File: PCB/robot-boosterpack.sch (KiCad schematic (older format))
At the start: 17 parts

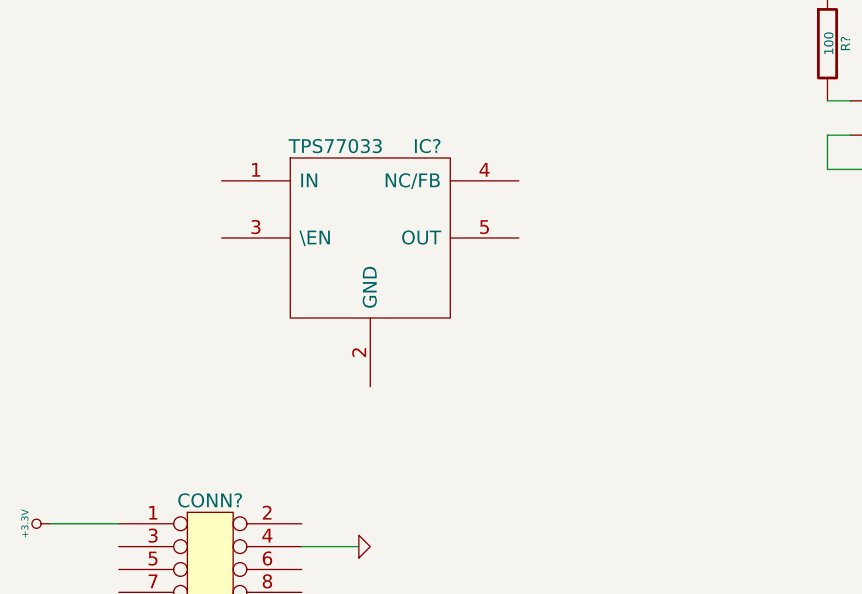
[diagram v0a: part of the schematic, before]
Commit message: created 3.3V regulator circuit
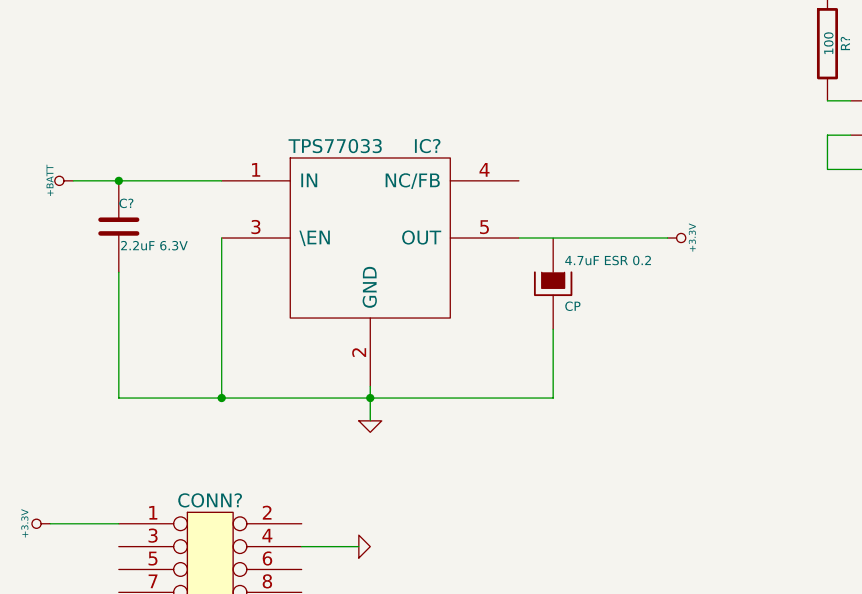
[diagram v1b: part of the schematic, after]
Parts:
- added 4.7uF: CP, symbol CP
- added C?: 2.2uF 6.3V, ~, symbol C
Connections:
- wire segments 43 -> 50
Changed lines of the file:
@@
 	1    0    0    -1
 $EndComp
+$Comp
+L C C?
+U 1 1 53A8AF20
+P 3600 1850
+F 0 "C?" H 3600 1950 40  0000 L CNN
+F 1 "2.2uF 6.3V" H 3606 1765 40  0000 L CNN
+F 2 "~" H 3638 1700 30  0000 C CNN
+F 3 "~" H 3600 1850 60  0000 C CNN
+	1    3600 1850
+	1    0    0    -1
+$EndComp
+Wire Wire Line
+	3400 1650 4050 1650
+Connection ~ 3600 1650
+Wire Wire Line
+	4700 2550 4700 2700
+Wire Wire Line
+	3600 2600 5500 2600
+Wire Wire Line
+	3600 2600 3600 2050
+Wire Wire Line
+	4050 1900 4050 2600
+Connection ~ 4050 2600
+$Comp
+L GND #PWR?
+U 1 1 53A8B23A
+P 4700 2700
+F 0 "#PWR?" H 4700 2700 30  0001 C CNN
+F 1 "GND" H 4700 2630 30  0001 C CNN
+F 2 "" H 4700 2700 60  0000 C CNN
+F 3 "" H 4700 2700 60  0000 C CNN
+	1    4700 2700
+	1    0    0    -1
+$EndComp
+Connection ~ 4700 2600
+Wire Wire Line
+	5350 1900 6000 1900
+$Comp
+L CP 4.7uF
+U 1 1 53A8B338
+P 5500 2100
+F 0 "4.7uF ESR 0.2" H 5550 2200 40  0000 L CNN
+F 1 "CP" H 5550 2000 40  0000 L CNN
+F 2 "" H 5600 1950 30  0000 C CNN
+F 3 "" H 5500 2100 300 0000 C CNN
+	1    5500 2100
+	1    0    0    -1
+$EndComp
+Wire Wire Line
+	5500 2600 5500 2300
+$Comp
+L +BATT #PWR?
+U 1 1 53A8B63C
+P 3400 1650
+F 0 "#PWR?" H 3400 1600 20  0001 C CNN
+F 1 "+BATT" H 3400 1750 30  0000 C CNN
+F 2 "" H 3400 1650 60  0000 C CNN
+F 3 "" H 3400 1650 60  0000 C CNN
+	1    3400 1650
+	0    -1   -1   0
+$EndComp
+$Comp
+L +3.3V #PWR?
+U 1 1 53A8B835
+P 6000 1900
+F 0 "#PWR?" H 6000 1860 30  0001 C CNN
+F 1 "+3.3V" H 6000 2010 30  0000 C CNN
+F 2 "" H 6000 1900 60  0000 C CNN
+F 3 "" H 6000 1900 60  0000 C CNN
+	1    6000 1900
+	0    1    1    0
+$EndComp
 $EndSCHEMATC

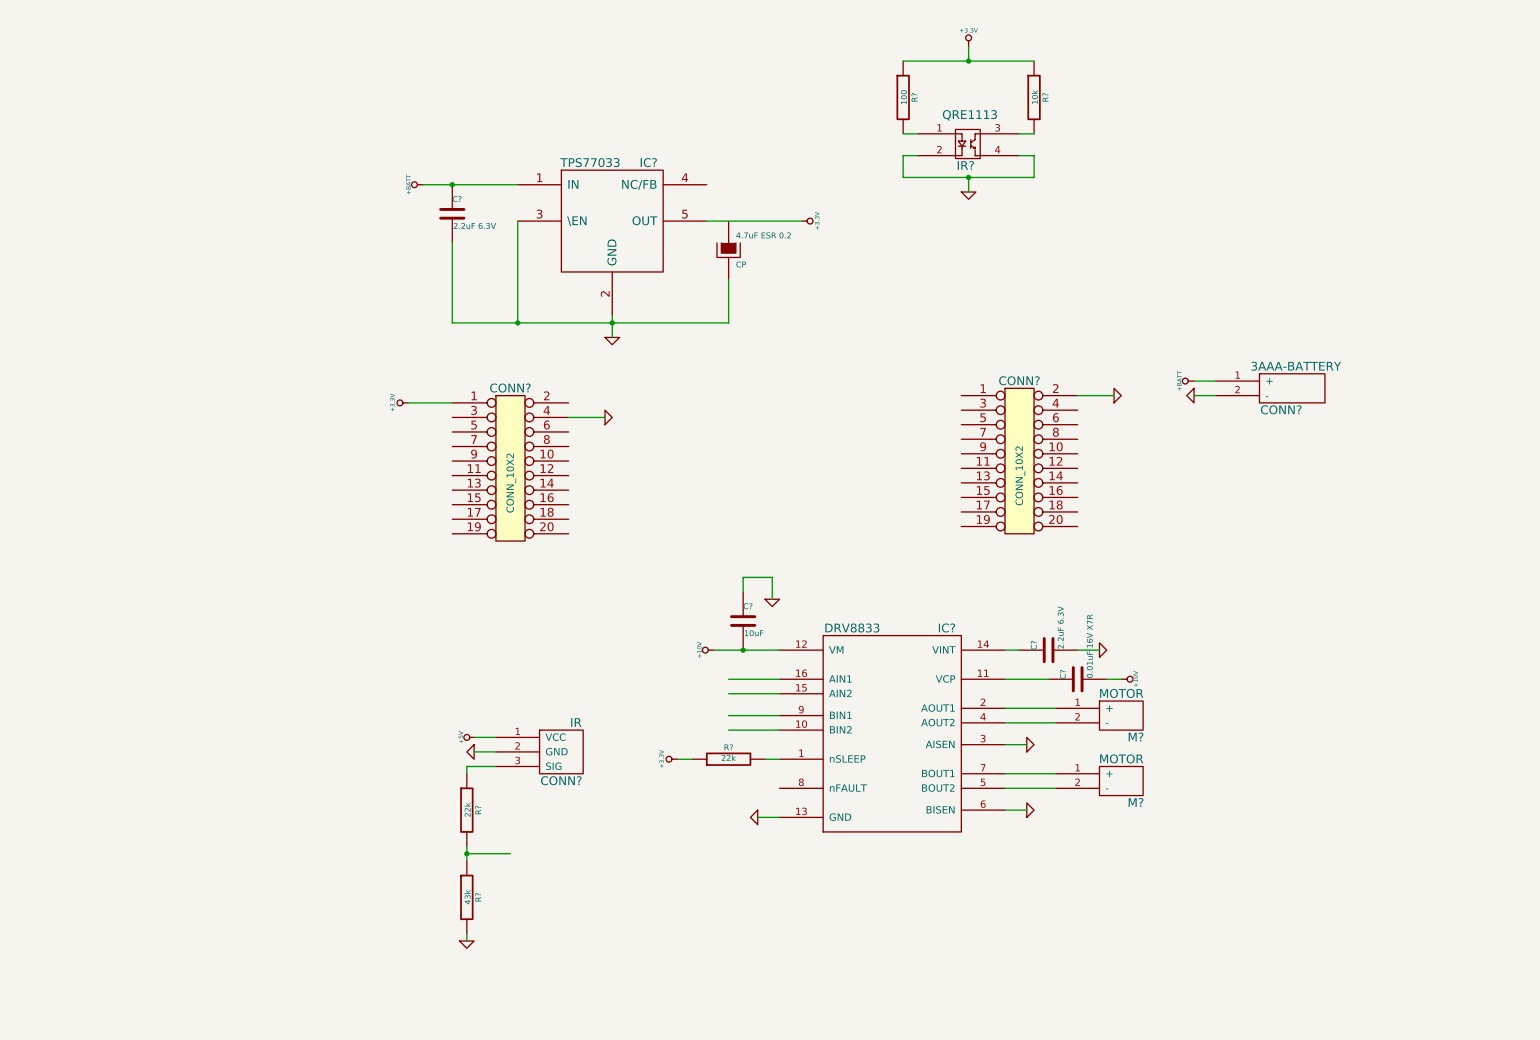
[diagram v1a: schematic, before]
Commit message: created 10V regulator schematic
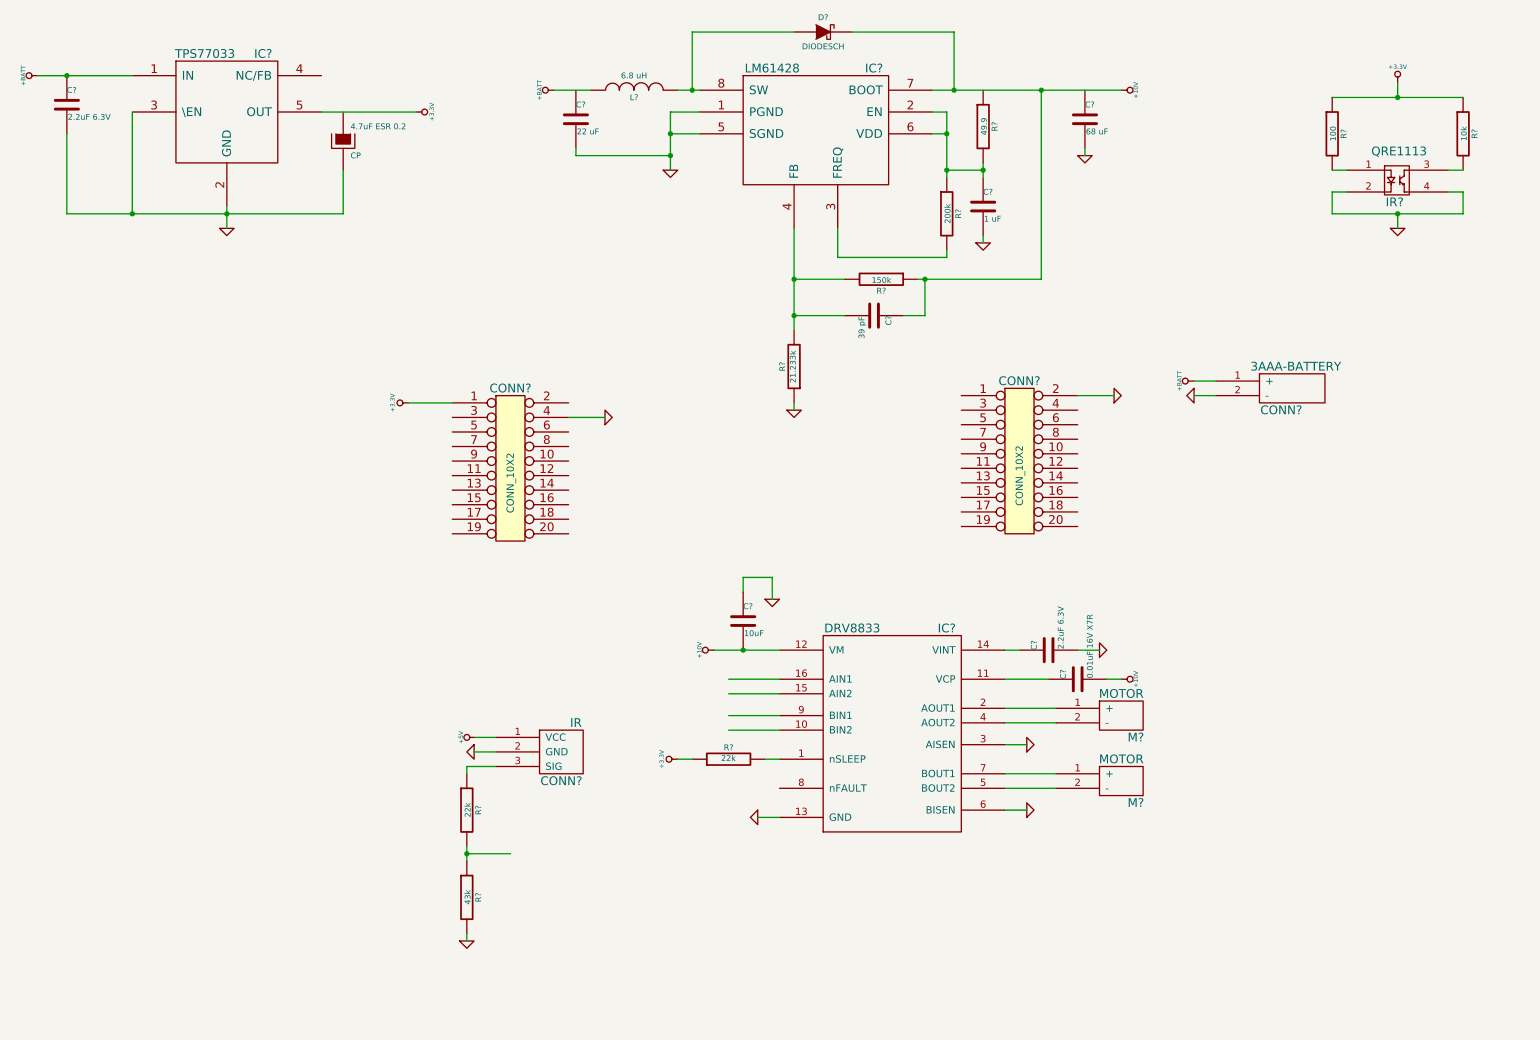
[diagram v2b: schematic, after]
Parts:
- added C?: 22 uF, ~, symbol C
- added C?: 1 uF, ~, symbol C
- added C?: 39 pF, ~, symbol C
- added C?: 68 uF, ~, symbol C
- added D?: DIODESCH, symbol DIODESCH
- added IC?: LM61428, symbol LM61428
- added L?: 6.8 uH, symbol INDUCTOR
- added R?: 49.9, ~, symbol R
- added R?: 200k, ~, symbol R
- added R?: 150k, ~, symbol R
- added R?: 21.233k, ~, symbol R
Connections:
- wire segments 50 -> 80
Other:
- moved on the sheet: 4.7uF ESR 0.2, C?, IC?, IR?, R?

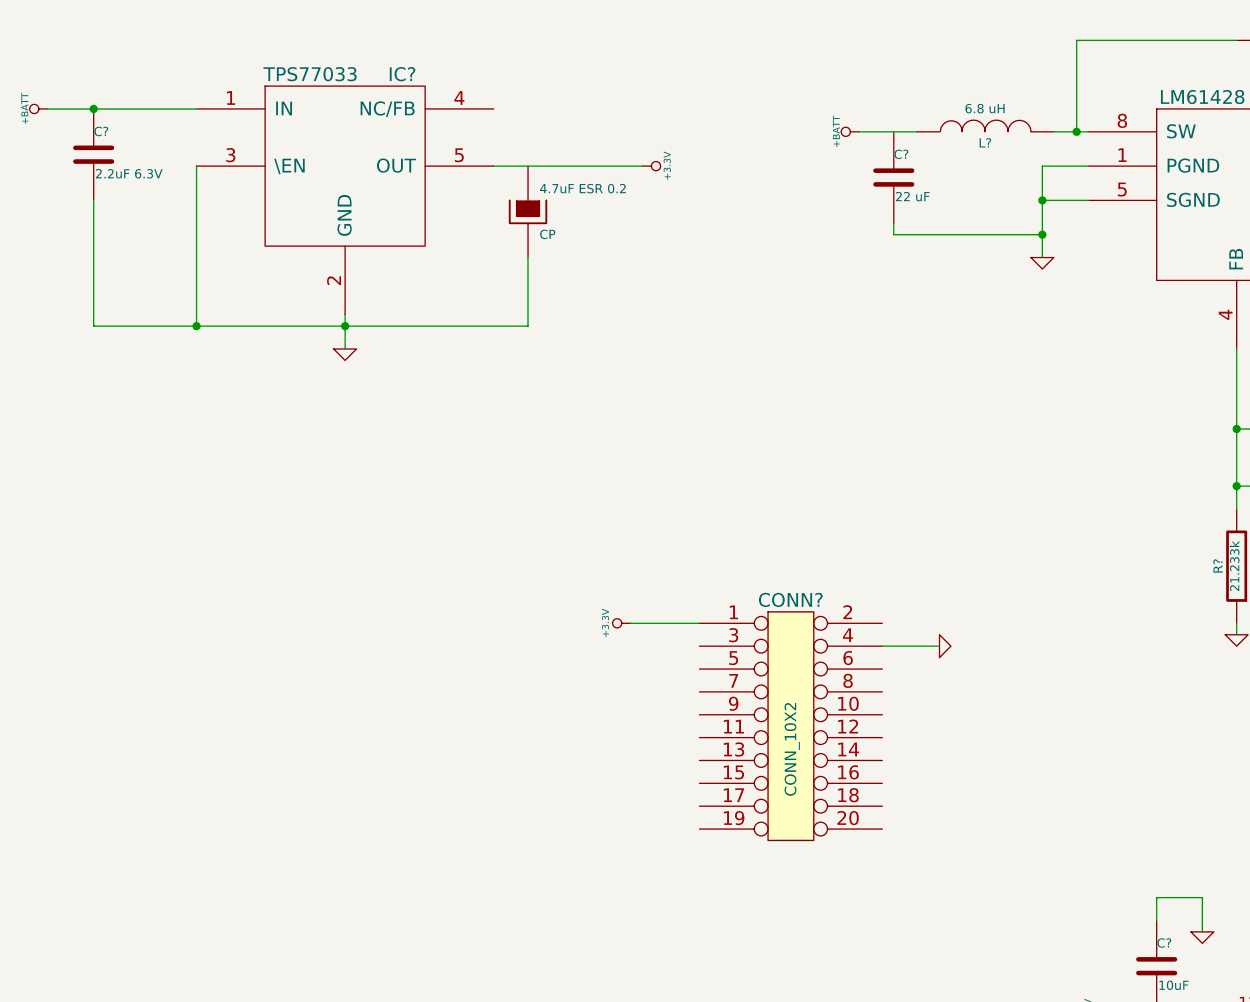
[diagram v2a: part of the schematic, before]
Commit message: added 5V regulator circuit
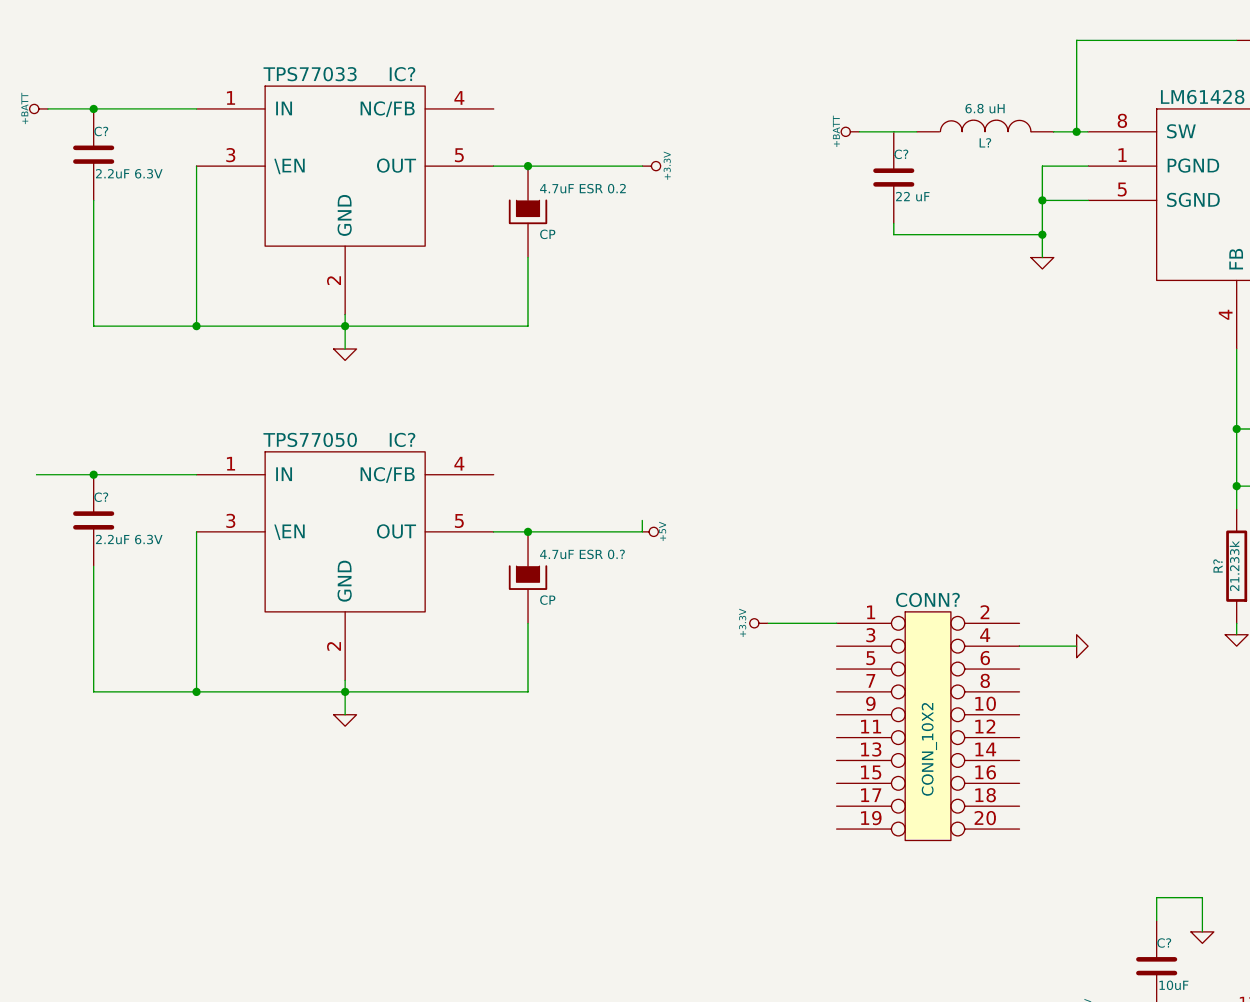
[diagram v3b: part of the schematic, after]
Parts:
- added 4.7uF~ESR~0.?: CP, symbol CP
- added C?: 2.2uF 6.3V, ~, symbol C
- added IC?: TPS77050, symbol TPS77050
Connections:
- wire segments 80 -> 88
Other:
- moved on the sheet: CONN?
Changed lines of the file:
@@
 L CONN_10X2 CONN?
 U 1 1 53A20530
-P 4000 3600
-F 0 "CONN?" H 4000 4150 60  0000 C CNN
-F 1 "CONN_10X2" V 4000 3500 50  0000 C CNN
-F 2 "" H 4000 3600 60  0000 C CNN
-F 3 "" H 4000 3600 60  0000 C CNN
-	1    4000 3600
+P 4600 3600
+F 0 "CONN?" H 4600 4150 60  0000 C CNN
+F 1 "CONN_10X2" V 4600 3500 50  0000 C CNN
+F 2 "" H 4600 3600 60  0000 C CNN
+F 3 "" H 4600 3600 60  0000 C CNN
+	1    4600 3600
 	1    0    0    -1
 $EndComp
@@
 L +3.3V #PWR?
 U 1 1 53A7389D
-P 3300 3150
-F 0 "#PWR?" H 3300 3110 30  0001 C CNN
-F 1 "+3.3V" H 3300 3260 30  0000 C CNN
-F 2 "" H 3300 3150 60  0000 C CNN
-F 3 "" H 3300 3150 60  0000 C CNN
-	1    3300 3150
+P 3900 3150
+F 0 "#PWR?" H 3900 3110 30  0001 C CNN
+F 1 "+3.3V" H 3900 3260 30  0000 C CNN
+F 2 "" H 3900 3150 60  0000 C CNN
+F 3 "" H 3900 3150 60  0000 C CNN
+	1    3900 3150
 	0    -1   -1   0
 $EndComp
@@
 L GND #PWR?
 U 1 1 53A738AC
-P 4650 3250
-F 0 "#PWR?" H 4650 3250 30  0001 C CNN
-F 1 "GND" H 4650 3180 30  0001 C CNN
-F 2 "" H 4650 3250 60  0000 C CNN
-F 3 "" H 4650 3250 60  0000 C CNN
-	1    4650 3250
+P 5250 3250
+F 0 "#PWR?" H 5250 3250 30  0001 C CNN
+F 1 "GND" H 5250 3180 30  0001 C CNN
+F 2 "" H 5250 3250 60  0000 C CNN
+F 3 "" H 5250 3250 60  0000 C CNN
+	1    5250 3250
 	0    -1   -1   0
 $EndComp
@@
 	7400 5800 7750 5800
 Wire Wire Line
-	4400 3250 4650 3250
-Wire Wire Line
-	3300 3150 3600 3150
+	5000 3250 5250 3250
+Wire Wire Line
+	3900 3150 4200 3150
 Wire Wire Line
 	7900 3100 8150 3100
@@
 Wire Wire Line
 	750  900  1400 900
-Connection ~ 950  900
 Wire Wire Line
 	2050 1800 2050 1950
@@
 Wire Wire Line
 	7950 1400 7950 1450
+$Comp
+L TPS77050 IC?
+U 1 1 53A9EB1D
+P 2050 2650
+F 0 "IC?" H 2300 2950 60  0000 C CNN
+F 1 "TPS77050" H 1900 2950 60  0000 C CNN
+F 2 "" H 1900 2950 60  0000 C CNN
+F 3 "" H 1900 2950 60  0000 C CNN
+	1    2050 2650
+	1    0    0    -1
+$EndComp
+$Comp
+L C C?
+U 1 1 53A9EDDD
+P 950 2700
+F 0 "C?" H 950 2800 40  0000 L CNN
+F 1 "2.2uF 6.3V" H 956 2615 40  0000 L CNN
+F 2 "~" H 988 2550 30  0000 C CNN
+F 3 "~" H 950 2700 60  0000 C CNN
+	1    950  2700
+	1    0    0    -1
+$EndComp
+$Comp
+L CP 4.7uF~ESR~0.?
+U 1 1 53A9EE61
+P 2850 2950
+F 0 "4.7uF ESR 0.?" H 2900 3050 40  0000 L CNN
+F 1 "CP" H 2900 2850 40  0000 L CNN
+F 2 "" H 2950 2800 30  0000 C CNN
+F 3 "" H 2850 2950 300 0000 C CNN
+	1    2850 2950
+	1    0    0    -1
+$EndComp
+Wire Wire Line
+	1400 2500 700  2500
+Connection ~ 950  2500
+$Comp
+L GND #PWR?
+U 1 1 53A9F331
+P 2050 3550
+F 0 "#PWR?" H 2050 3550 30  0001 C CNN
+F 1 "GND" H 2050 3480 30  0001 C CNN
+F 2 "" H 2050 3550 60  0000 C CNN
+F 3 "" H 2050 3550 60  0000 C CNN
+	1    2050 3550
+	1    0    0    -1
+$EndComp
+Wire Wire Line
+	2050 3400 2050 3550
+Wire Wire Line
+	950  3450 2850 3450
+Wire Wire Line
+	950  3450 950  2900
+Wire Wire Line
+	1400 2750 1400 3450
+Connection ~ 1400 3450
+Wire Wire Line
+	2850 3450 2850 3150
+Connection ~ 2050 3450
+Wire Wire Line
+	2700 2750 3350 2750
+$Comp
+L +5V #PWR?
+U 1 1 53A9F6C1
+P 3350 2750
+F 0 "#PWR?" H 3350 2840 20  0001 C CNN
+F 1 "+5V" H 3350 2840 30  0000 C CNN
+F 2 "" H 3350 2750 60  0000 C CNN
+F 3 "" H 3350 2750 60  0000 C CNN
+	1    3350 2750
+	0    1    1    0
+$EndComp
+Wire Wire Line
+	3350 2750 3350 2700
+Connection ~ 2850 2750
+Connection ~ 950  900
+Connection ~ 2850 1150
 $EndSCHEMATC
